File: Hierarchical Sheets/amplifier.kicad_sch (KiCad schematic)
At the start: 3 parts, among them U2 ${SIM.PARAMS}

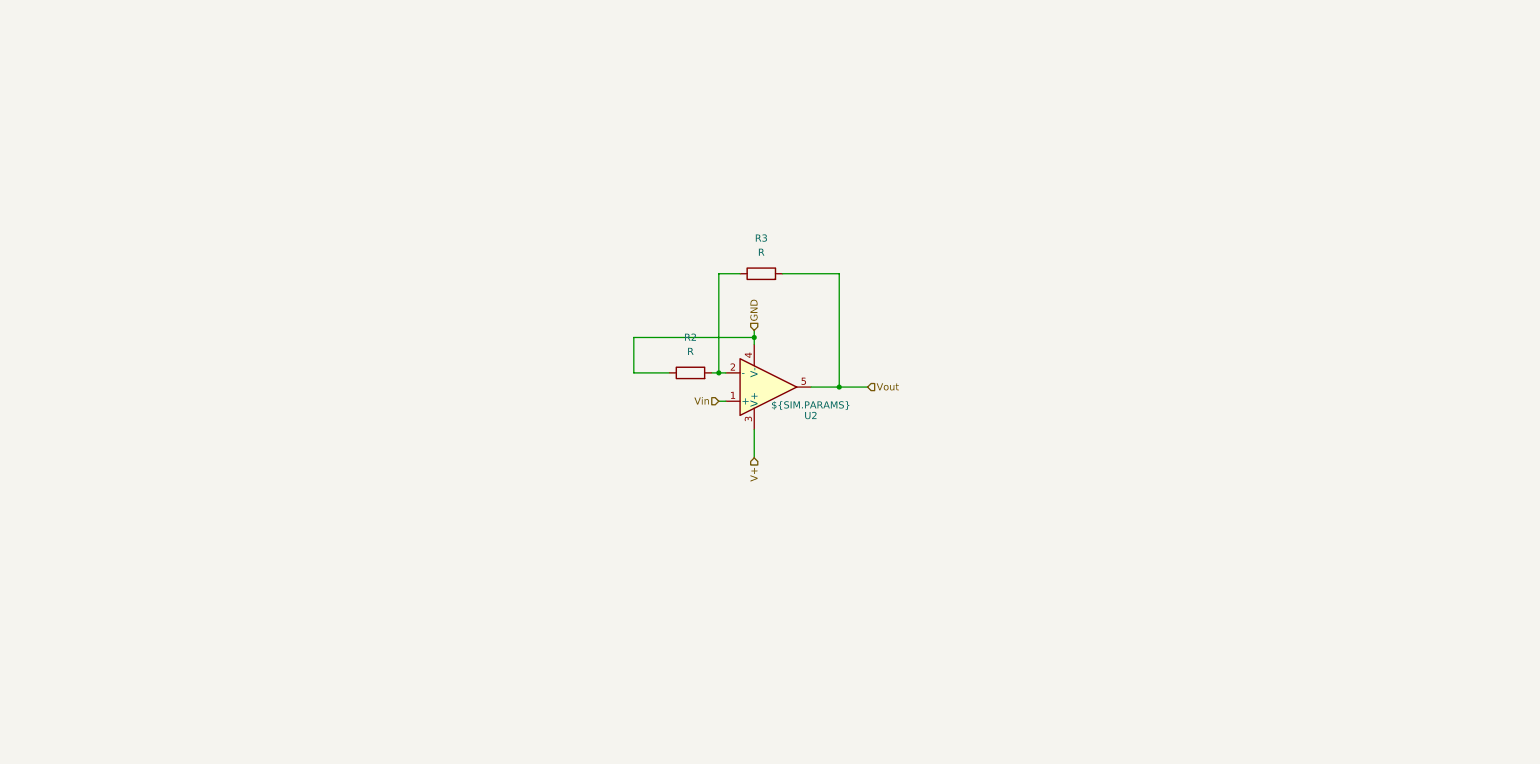
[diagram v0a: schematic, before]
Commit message: remove Hierarchical Sheets folder inside Hierarchical Sheets foler
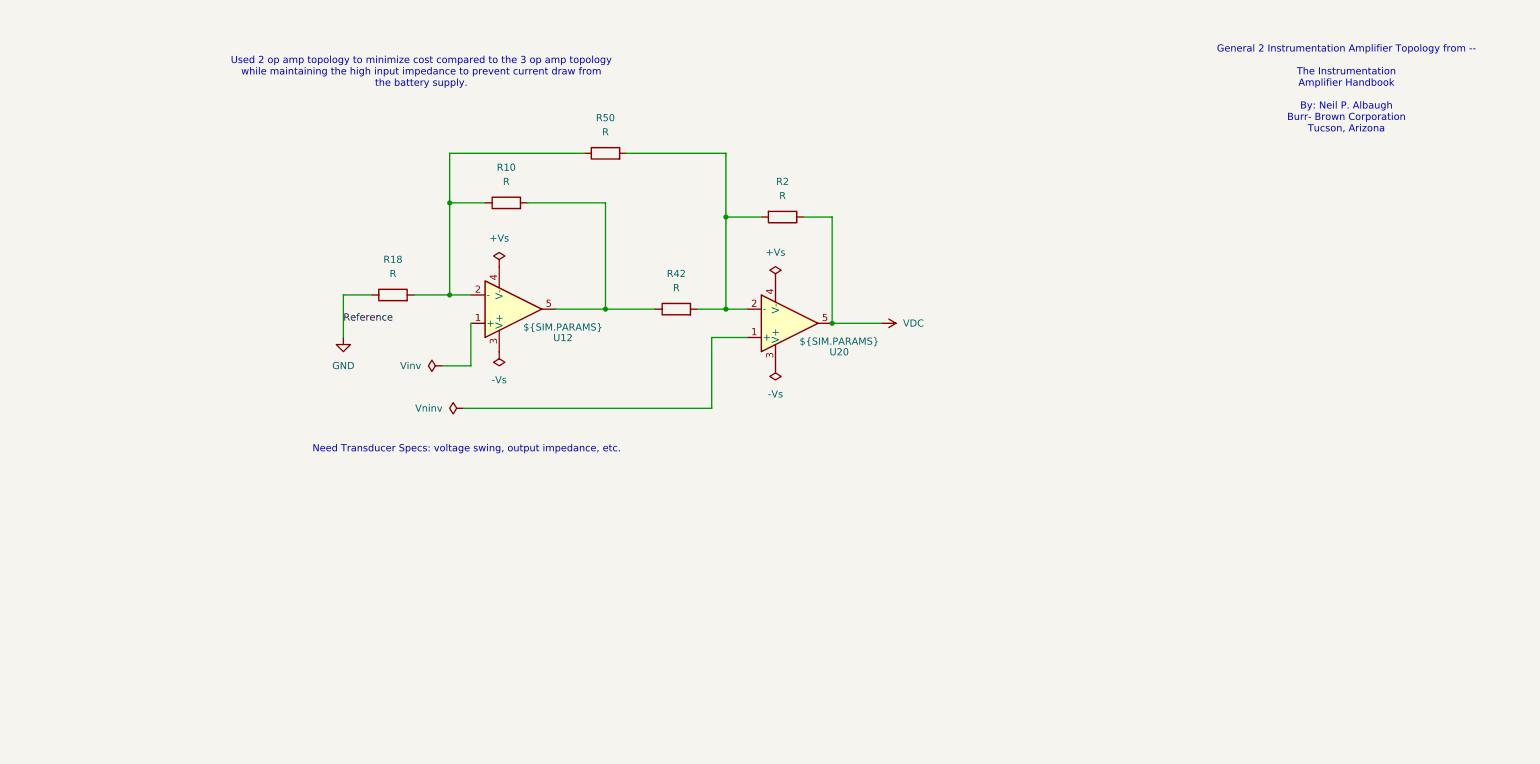
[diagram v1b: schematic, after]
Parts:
- removed R3: R, Resistor_SMD:R_0201_0603Metric_Pad0.64x0.40mm_HandSolder, symbol Device:R
- removed U2: ${SIM.PARAMS}, Package_SO:SOIC-8-1EP_3.9x4.9mm_P1.27mm_EP2.29x3mm, symbol Simulation_SPICE:OPAMP
- added R10: R, Resistor_SMD:R_0201_0603Metric_Pad0.64x0.40mm_HandSolder, symbol Device:R
- added R18, R42, R50: R, symbol Device:R
- added U12, U20: ${SIM.PARAMS}, symbol Simulation_SPICE:OPAMP
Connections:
- net GND: now also R18.1; no longer R2.1
- net at R2.2: now also R42.2, R50.2, U20.2 (-)
- new net: R10.1, R18.2, R50.1, U12.2 (-)
- new net: R10.2, R42.1, U12.5
- new net VDC: R2.1, U20.5
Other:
- note added: "General 2 Instrumentation Amplifier Topology from -- The Instrumentation Amplifier Handbook By: Neil P. Albaugh Burr- Brown Corporation Tucson, Arizona"
- note added: "Need Transducer Specs: voltage swing, output impedance, etc."
- note added: "Used 2 op amp topology to minimize cost compared to the 3 op amp topology while maintaining the high input impedance to prevent current draw from the battery supply."

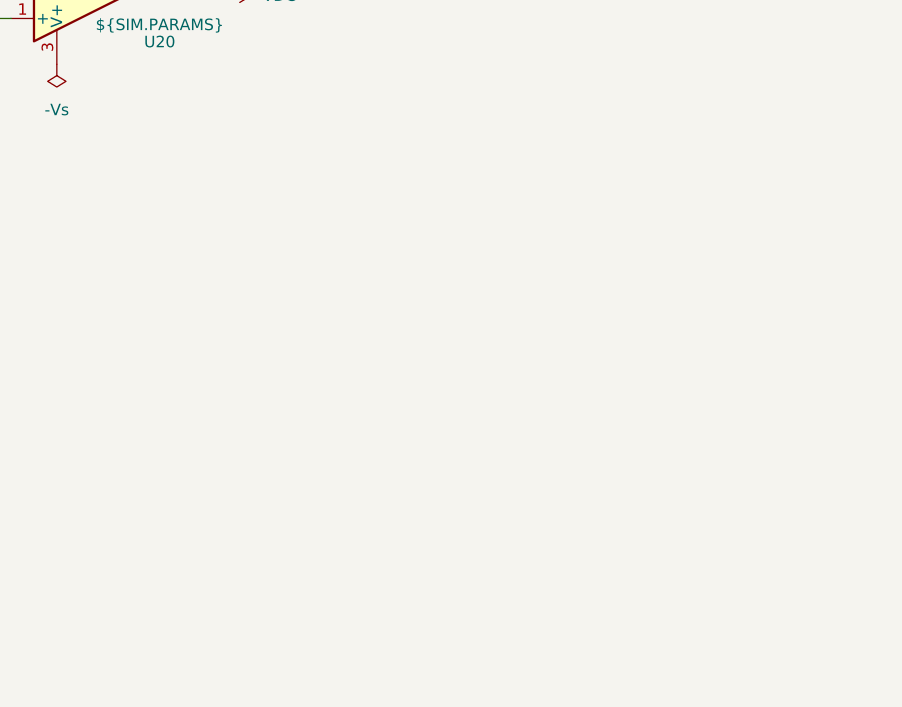
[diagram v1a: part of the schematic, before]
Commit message: Switched to pre-made instr. amp. - made preliminary choice of IA
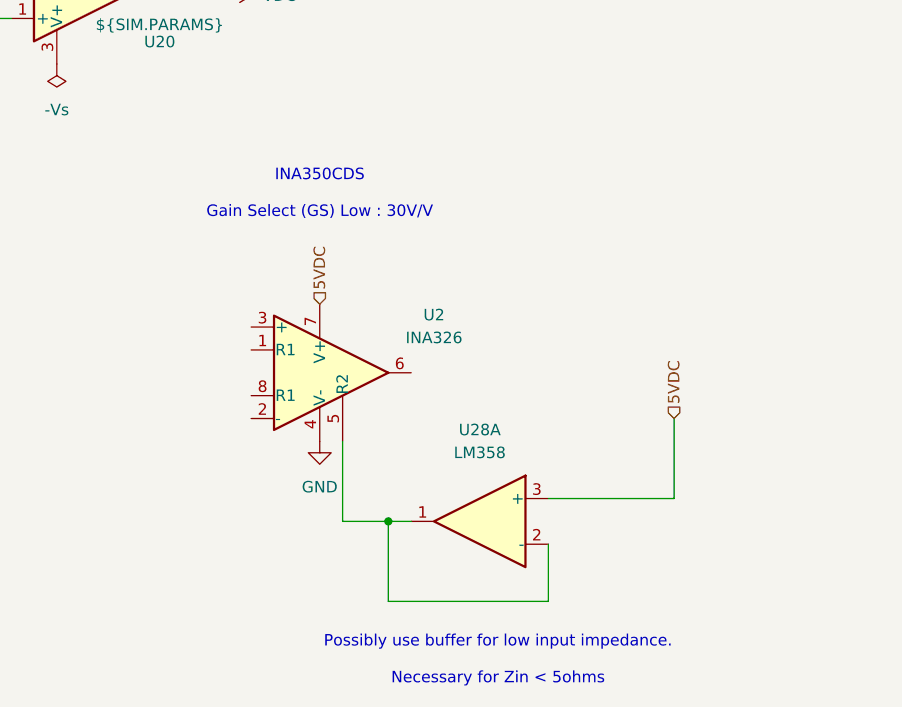
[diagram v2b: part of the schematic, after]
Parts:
- added U2: INA326, Package_SO:MSOP-8_3x3mm_P0.65mm, symbol Amplifier_Instrumentation:INA326
- added U28: LM358, symbol Amplifier_Operational:LM358
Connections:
- net GND: now also U2.4 (V-)
- new net: U2.5 (R2), U28.1, U28.2 (-)
- new net 5VDC: U2.7 (V+), U28.3 (+)
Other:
- note added: "INA350CDS Gain Select (GS) Low : 30V/V"
- note added: "Possibly use buffer for low input impedance. Necessary for Zin < 5ohms"

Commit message: changed the description on the buffer op amp in amplifier schematic
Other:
- note added: "Possibly use buffer for low input impedance at the REF pin. Necessary for Zin < 5ohms"
- note removed: "Possibly use buffer for low input impedance. Necessary for Zin < 5ohms"
- moved on the sheet: R10, R18, R2, R42, R50, U12, U2, U20, U28A

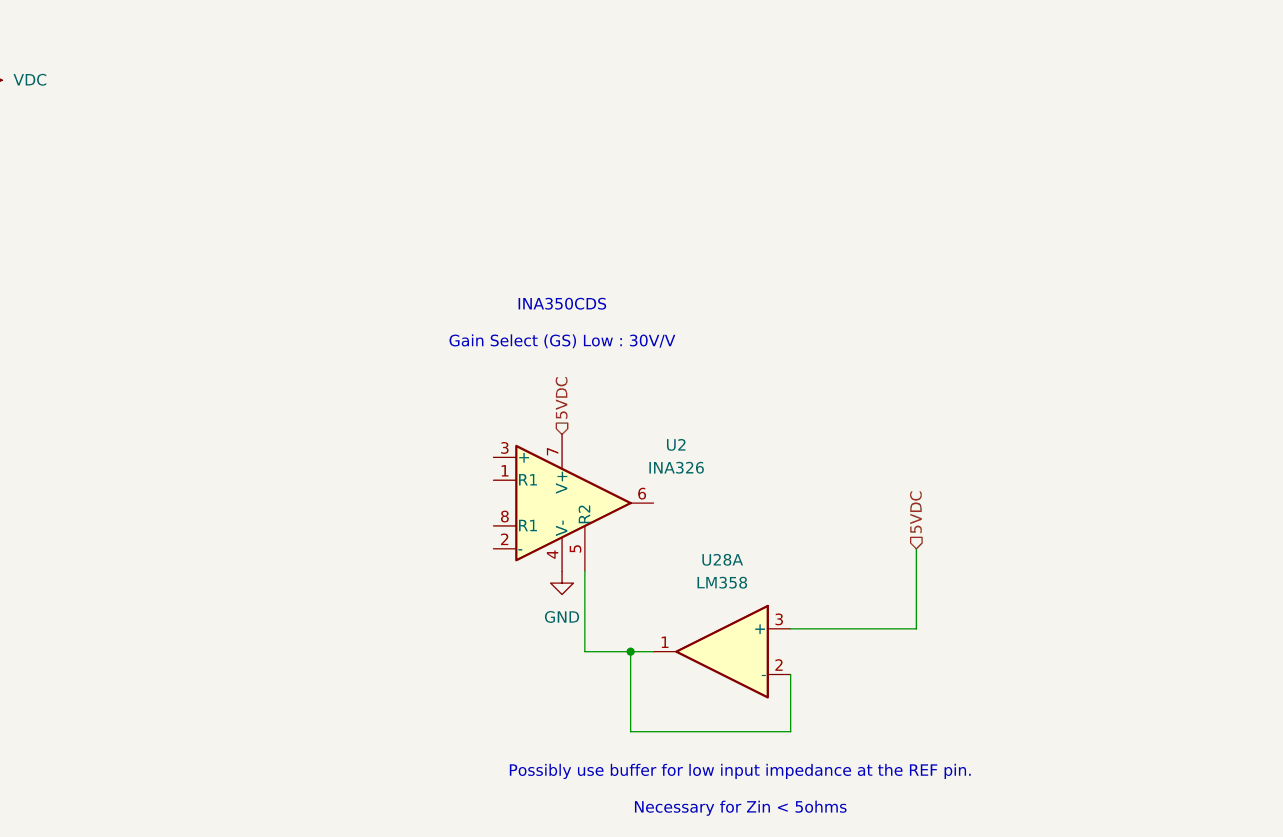
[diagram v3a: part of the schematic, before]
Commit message: Added new INA350CDS to part library and placed it into the schematic
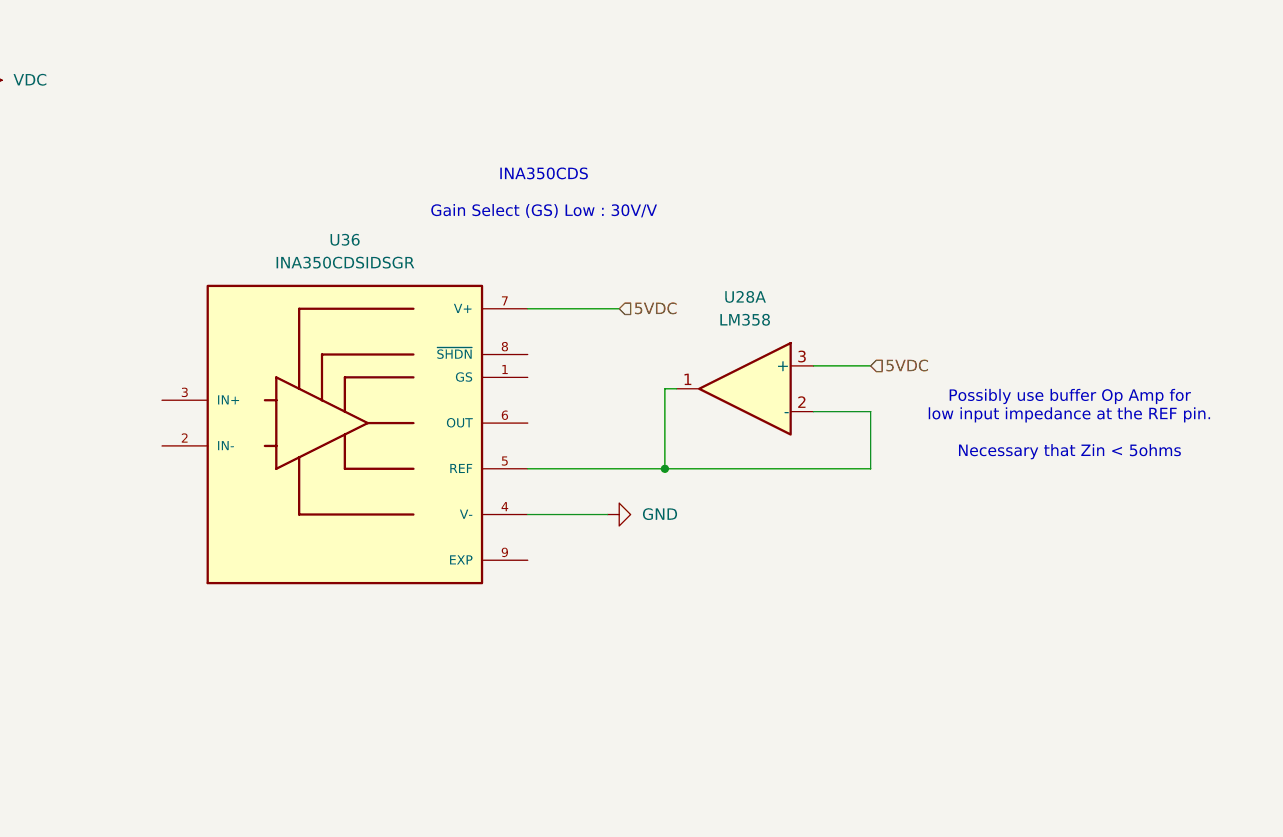
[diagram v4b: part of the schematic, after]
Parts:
- removed U2: INA326, Package_SO:MSOP-8_3x3mm_P0.65mm, symbol Amplifier_Instrumentation:INA326
- added U36: INA350CDSIDSGR, INA350CDSIDSGR:IC_INA350CDSIDSGR, symbol INA350CDSIDSGR:INA350CDSIDSGR
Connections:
- net 5VDC: now also U36.7 (V+)
- net GND: now also U36.4 (V-)
- net at U28.1, U28.2 (-): now also U36.5 (REF)
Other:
- note added: "Possibly use buffer Op Amp for low input impedance at the REF pin. Necessary that Zin < 5ohms"
- note removed: "Possibly use buffer for low input impedance at the REF pin. Necessary for Zin < 5ohms"
- moved on the sheet: U28A

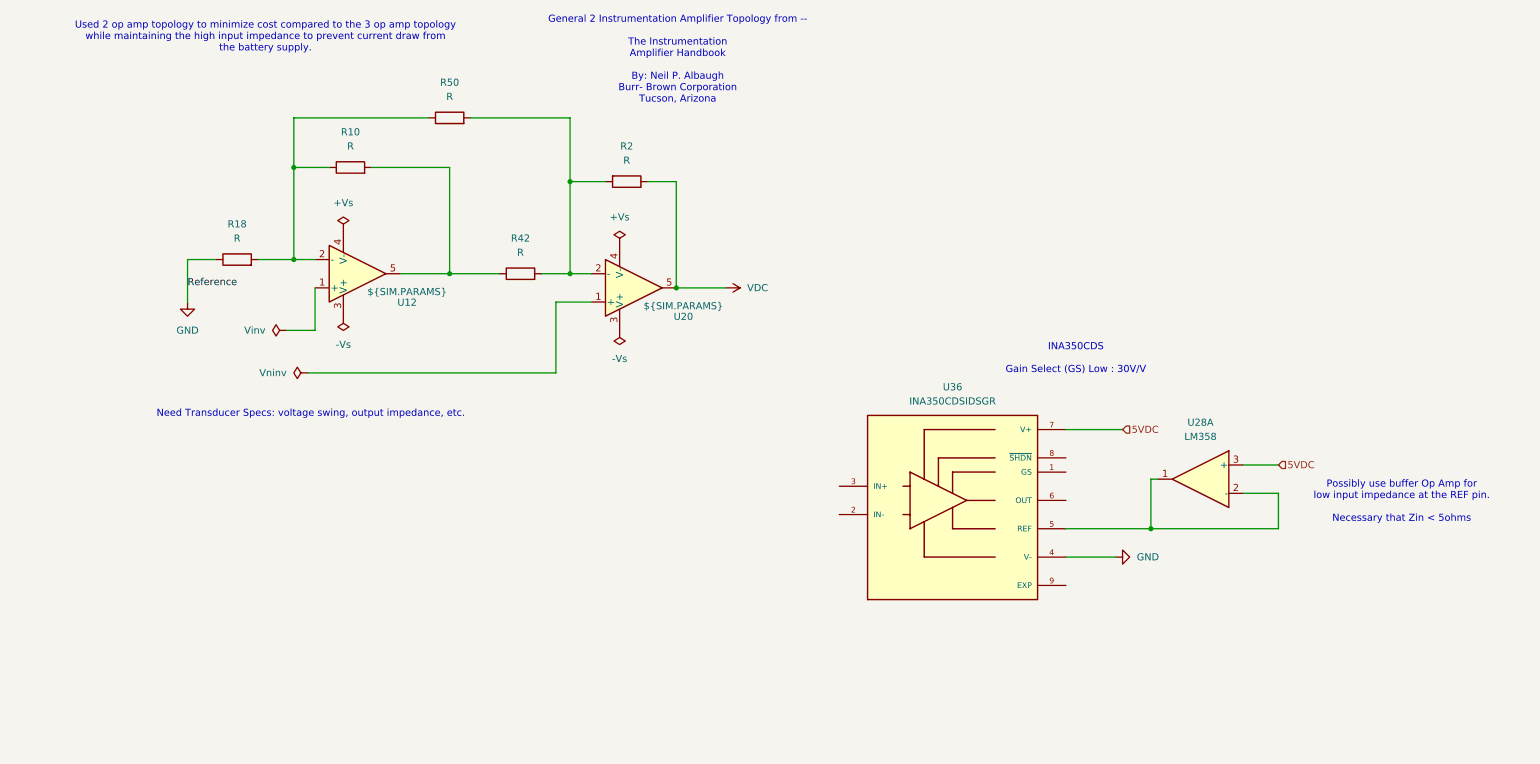
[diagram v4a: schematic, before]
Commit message: Added 2nd order low-pass filter topology - Still working on exact design
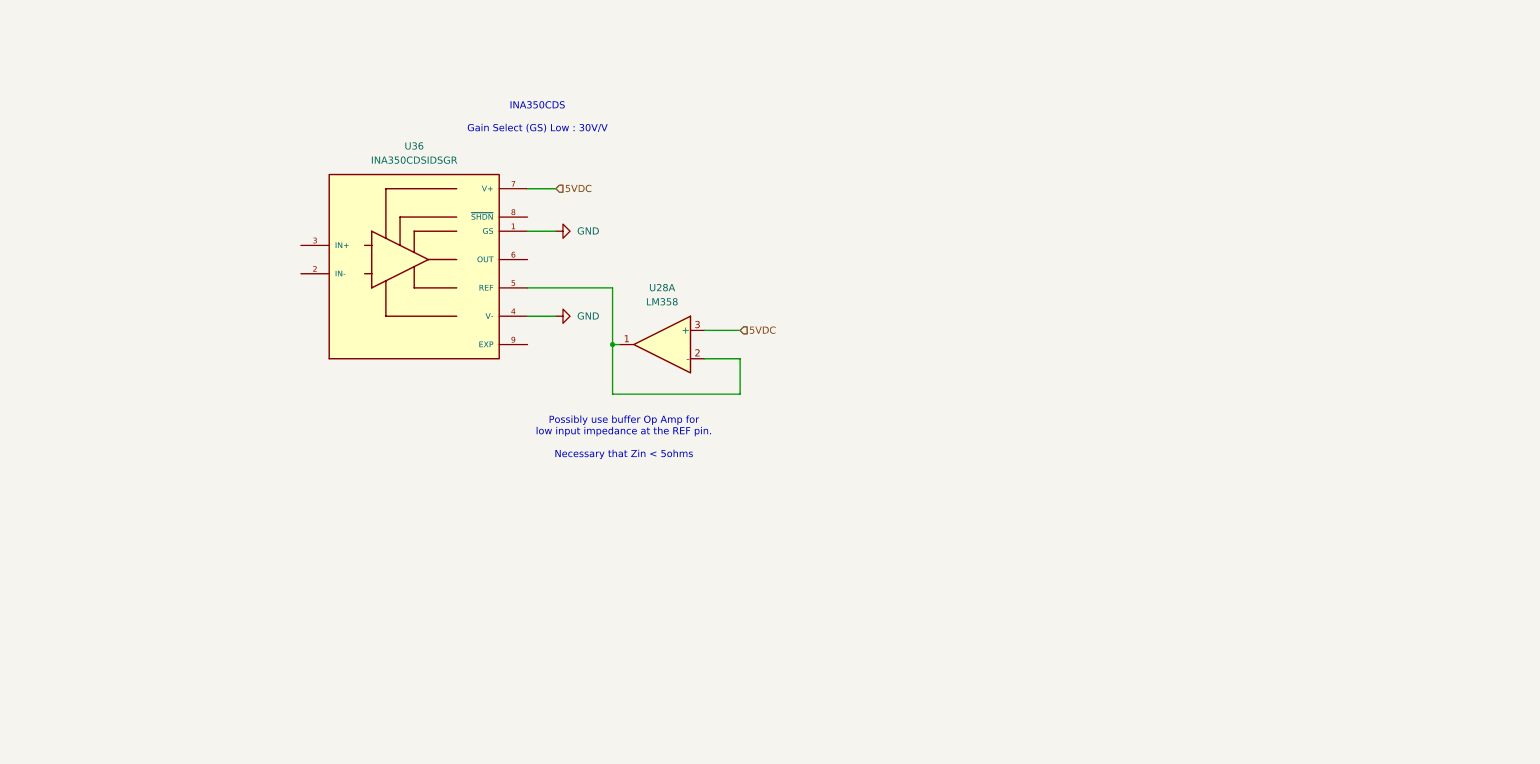
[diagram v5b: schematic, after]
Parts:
- removed R10, R2: R, Resistor_SMD:R_0201_0603Metric_Pad0.64x0.40mm_HandSolder, symbol Device:R
- removed R18, R42, R50: R, symbol Device:R
- removed U12, U20: ${SIM.PARAMS}, symbol Simulation_SPICE:OPAMP
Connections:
- net GND: now also U36.1 (GS)
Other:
- note removed: "General 2 Instrumentation Amplifier Topology from -- The Instrumentation Amplifier Handbook By: Neil P. Albaugh Burr- Brown Corporation Tucson, Arizona"
- note removed: "Need Transducer Specs: voltage swing, output impedance, etc."
- note removed: "Used 2 op amp topology to minimize cost compared to the 3 op amp topology while maintaining the high input impedance to prevent current draw from the battery supply."
- moved on the sheet: U28A, U36
